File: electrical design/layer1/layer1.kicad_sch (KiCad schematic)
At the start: 76 parts, among them SW1 SW_DPDT_x2, U1 STM32F103C8T6, U2 CD74HC4067SM, U3 CD74HC4067SM

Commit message: finish stm32f103c8t6 sub-circuit
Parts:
- added C4, C5, C6, C7: 1μF, symbol Device:C
- added C8, C9: 1pF, Capacitors:0603, symbol Device:C
- added D33: BLUE, symbol Device:LED
- added FB1, FB2: 30Ω/1.8A, symbol Device:FerriteBead
- added J1: Conn_01x08_Male, symbol Connector:Conn_01x08_Male
- added J2: Conn_01x06_Female, Connector_JST:JST_SH_BM06B-SRSS-TB_1x06-1MP_P1.00mm_Vertical, symbol Connector:Conn_01x06_Female
- added R38, R41: 10k, symbol Device:R
- added R39, R40: 1k, symbol Device:R
- added SW2: SW_DPDT_x2, symbol Switch:SW_DPDT_x2
- added SW3: SW_Push, symbol Switch:SW_Push
- added Y1: Crystal, Clocks:CRYSTAL-SMD-5X3.2-2PAD, symbol Device:Crystal
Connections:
- net +3V3: now also SW2.1 (A)
- net GND: now also U1.23 (VSS), U1.35 (VSS), U1.47 (VSS), C4.1, C5.1, C6.1, C8.1, C9.1, D33.1 (K), FB2.1, J2.1 (Pin_1), R38.2, R40.1
- net MUX1OUT: now also U1.10 (PA0); no longer U1.18 (PB0)
- net OSCIN: now also C8.2, Y1.2
- net OSCOUT: now also C9.2, Y1.1
- net S0: now also U1.18 (PB0); no longer U1.38 (PA15)
- net S1: now also U1.19 (PB1); no longer U1.39 (PB3)
- net S2: now also U1.20 (PB2); no longer U1.40 (PB4)
- net S3: now also U1.21 (PB10); no longer U1.41 (PB5)
- net VCCQ: now also U1.9 (VDDA), C7.1, FB1.2
- net DEBUGRX: now reaches U1.13 (PA3)
- net DEBUGRX: now also J2.6 (Pin_6)
- net DEBUGTX: now reaches U1.14 (PA4)
- net DEBUGTX: now also J2.5 (Pin_5)
- net at U1.15 (PA5): now also R39.1
- net MCU3V3: now reaches U1.24 (VDD)
- net MCU3V3: now also U1.36 (VDD), U1.48 (VDD), C4.2, C5.2, C6.2, FB1.1, R41.2, SW2.2 (B)
- net SWDIO: now reaches U1.34 (PA13)
- net SWDIO: now also J2.3 (Pin_3)
- net SWDCLOCK: now reaches U1.37 (PA14)
- net SWDCLOCK: now also J2.2 (Pin_2)
- net M3EA: now reaches U1.42 (PB6)
- net M3EA: now also J1.5 (Pin_5)
- net M3EB: now reaches U1.43 (PB7)
- net M3EB: now also J1.6 (Pin_6)
- net at U1.44 (BOOT0): now also R38.1
- net M4EA: now reaches U1.45 (PB8)
- net M4EA: now also J1.7 (Pin_7)
- net M4EB: now reaches U1.46 (PB9)
- net M4EB: now also J1.8 (Pin_8)
- net RESET: now reaches U1.7 (NRST)
- net RESET: now also R41.1, SW3.2
- net GNDA: now reaches U1.8 (VSSA)
- net GNDA: now also C7.2, FB2.2
- new net: D33.2 (A), R39.2
- new net: R40.2, SW3.1
- new net M1EA: J1.1 (Pin_1), U1.38 (PA15)
- new net M1EB: J1.2 (Pin_2), U1.39 (PB3)
- new net M2EA: J1.3 (Pin_3), U1.40 (PB4)
- new net M2EB: J1.4 (Pin_4), U1.41 (PB5)
- new net PROG3V3: J2.4 (Pin_4), SW2.3 (C)
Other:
- moved on the sheet: U1

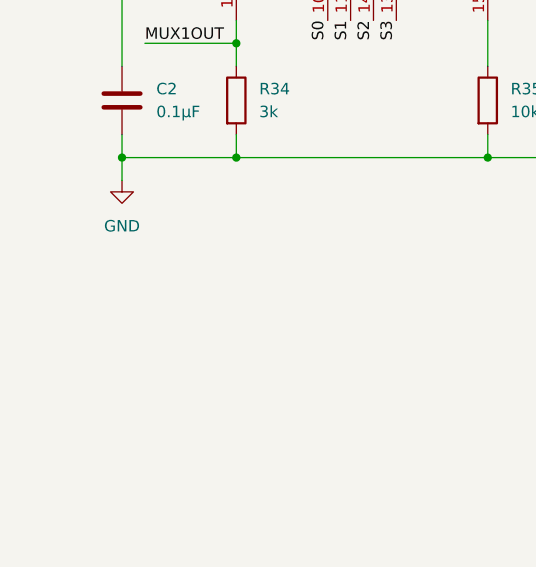
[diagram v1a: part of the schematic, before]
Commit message: add power input to layer 1
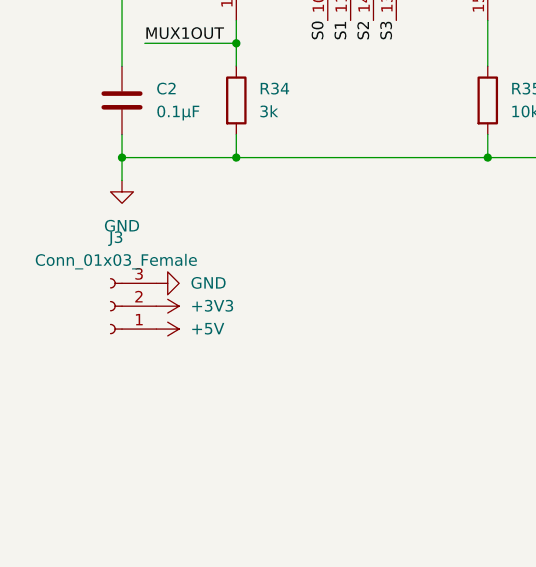
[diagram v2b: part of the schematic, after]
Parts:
- added J3: Conn_01x03_Female, symbol Connector:Conn_01x03_Female
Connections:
- net +3V3: now also J3.2 (Pin_2)
- net +5V: now also J3.1 (Pin_1)
- net GND: now also J3.3 (Pin_3)
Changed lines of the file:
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@@
+    (pin "1")
+  )
+  (symbol (lib_id "power:+5V") (at 25.4 119.38 270) (unit 1)
+    (in_bom yes) (on_board yes) (fields_autoplaced)
+    (property "Reference" "#PWR?" (id 0) (at 21.59 119.38 0)
+      (effects (font (size 1.27 1.27)) hide)
+    )
+    (property "Value" "+5V" (id 1) (at 29.21 119.3799 90)
+      (effects (font (size 1.27 1.27)) (justify left))
+    )
+    (property "Footprint" "" (id 2) (at 25.4 119.38 0)
+      (effects (font (size 1.27 1.27)) hide)
+    )
+    (property "Datasheet" "" (id 3) (at 25.4 119.38 0)
+      (effects (font (size 1.27 1.27)) hide)
+    )
     (pin "1")
   )
@@
     (pin "1")
     (pin "2")
+  )
+  (symbol (lib_id "power:GND") (at 25.4 114.3 90) (unit 1)
+    (in_bom yes) (on_board yes) (fields_autoplaced)
+    (property "Reference" "#PWR?" (id 0) (at 31.75 114.3 0)
+      (effects (font (size 1.27 1.27)) hide)
+    )
+    (property "Value" "GND" (id 1) (at 29.21 114.2999 90)
+      (effects (font (size 1.27 1.27)) (justify right))
+    )
+    (property "Footprint" "" (id 2) (at 25.4 114.3 0)
+      (effects (font (size 1.27 1.27)) hide)
+    )
+    (property "Datasheet" "" (id 3) (at 25.4 114.3 0)
+      (effects (font (size 1.27 1.27)) hide)
+    )
+    (pin "1")
   )
   (symbol (lib_id "Device:LED") (at 58.42 29.21 90) (unit 1)
@@
     (pin "1")
     (pin "2")
+  )
+  (symbol (lib_id "Connector:Conn_01x03_Female") (at 20.32 116.84 180) (unit 1)
+    (in_bom yes) (on_board yes) (fields_autoplaced)
+    (property "Reference" "J3" (id 0) (at 20.955 109.22 0))
+    (property "Value" "Conn_01x03_Female" (id 1) (at 20.955 111.76 0))
+    (property "Footprint" "" (id 2) (at 20.32 116.84 0)
+      (effects (font (size 1.27 1.27)) hide)
+    )
+    (property "Datasheet" "~" (id 3) (at 20.32 116.84 0)
+      (effects (font (size 1.27 1.27)) hide)
+    )
+    (pin "1")
+    (pin "2")
+    (pin "3")
   )
   (symbol (lib_id "power:+3V3") (at 199.39 45.72 0) (unit 1)
@@
     (pin "2")
   )
+  (symbol (lib_id "power:+3V3") (at 25.4 116.84 270) (unit 1)
+    (in_bom yes) (on_board yes) (fields_autoplaced)
+    (property "Reference" "#PWR?" (id 0) (at 21.59 116.84 0)
+      (effects (font (size 1.27 1.27)) hide)
+    )
+    (property "Value" "+3V3" (id 1) (at 29.21 116.8399 90)
+      (effects (font (size 1.27 1.27)) (justify left))
+    )
+    (property "Footprint" "" (id 2) (at 25.4 116.84 0)
+      (effects (font (size 1.27 1.27)) hide)
+    )
+    (property "Datasheet" "" (id 3) (at 25.4 116.84 0)
+      (effects (font (size 1.27 1.27)) hide)
+    )
+    (pin "1")
+  )
   (symbol (lib_id "power:GND") (at 250.19 88.9 90) (unit 1)
     (in_bom yes) (on_board yes) (fields_autoplaced)
@@
       (reference "#PWR019") (unit 1) (value "GND") (footprint "")
     )
+    (path "/2aea5601-d7e4-47c3-b7da-c0e856d55909"
+      (reference "#PWR?") (unit 1) (value "+5V") (footprint "")
+    )
+    (path "/60abfe79-9e86-41a9-b7e0-8fd3a8368518"
+      (reference "#PWR?") (unit 1) (value "GND") (footprint "")
+    )
+    (path "/e4c96178-3b79-4857-8901-bb58c069c644"
+      (reference "#PWR?") (unit 1) (value "+3V3") (footprint "")
+    )
     (path "/ee008ec7-5fc9-464d-9c4e-134d12caadc8"
       (reference "C1") (unit 1) (value "1μF") (footprint "")
@@
       (reference "J2") (unit 1) (value "Conn_01x06_Female") (footprint "Connector_JST:JST_SH_BM06B-SRSS-TB_1x06-1MP_P1.00mm_Vertical")
     )
+    (path "/86937535-1a00-4375-a966-feffacfd480e"
+      (reference "J3") (unit 1) (value "Conn_01x03_Female") (footprint "")
+    )
     (path "/fa77eeda-ce5b-40dc-b111-3164550acfac"
